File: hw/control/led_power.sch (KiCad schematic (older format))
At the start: 0 parts

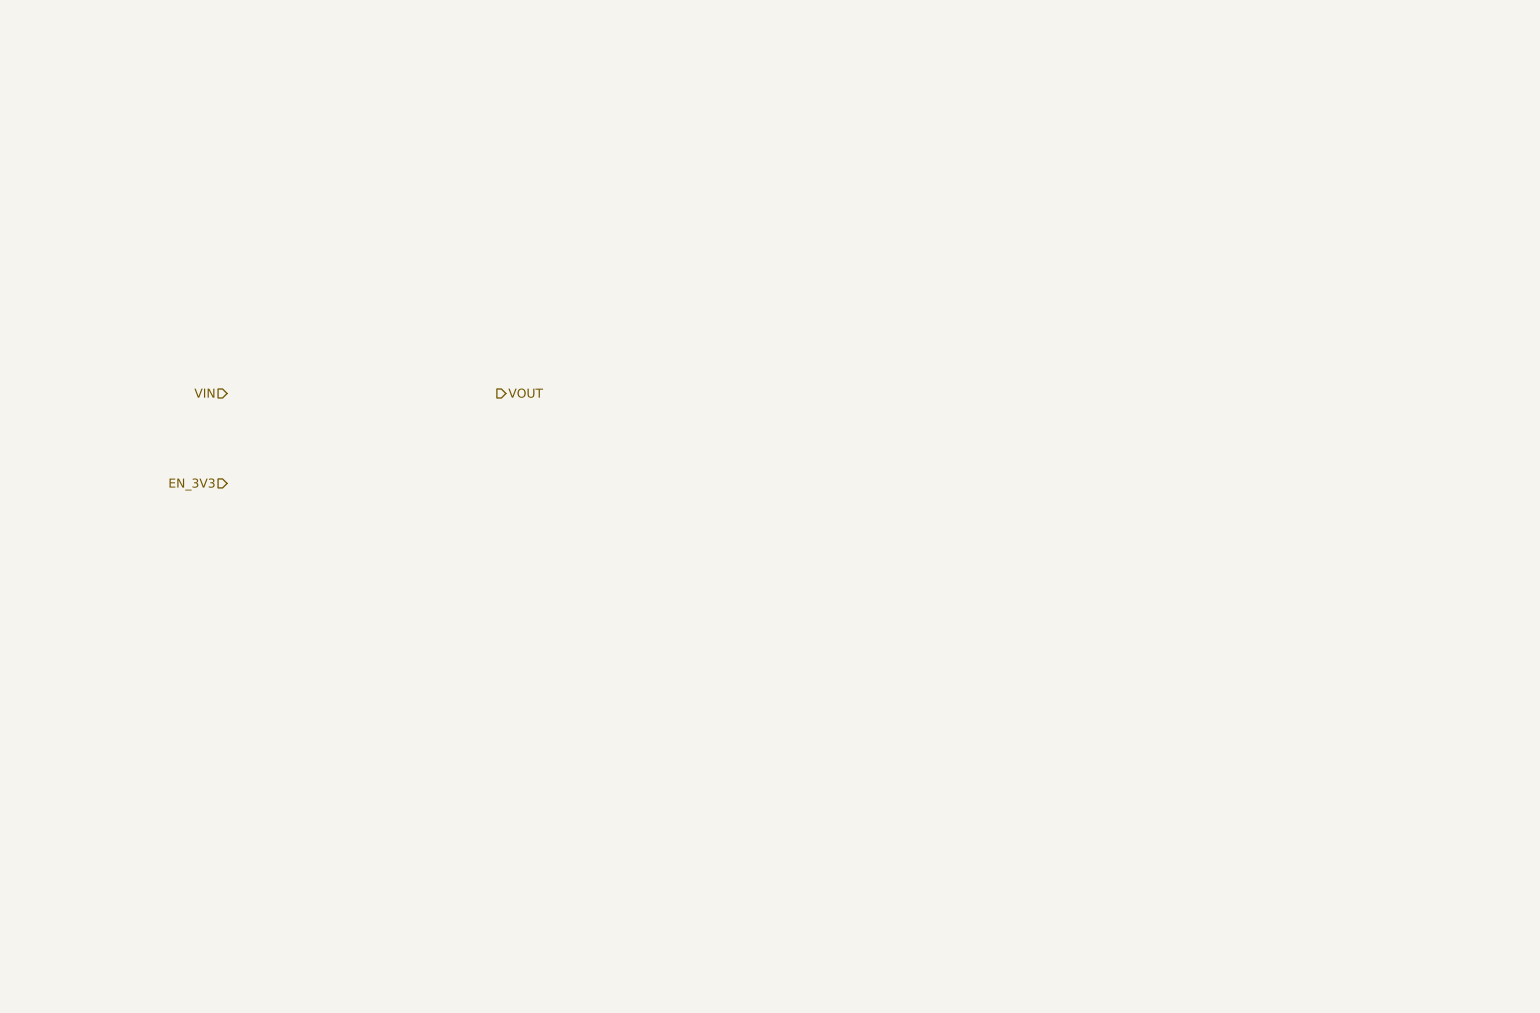
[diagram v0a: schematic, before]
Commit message: [hw] Sketch the input protection
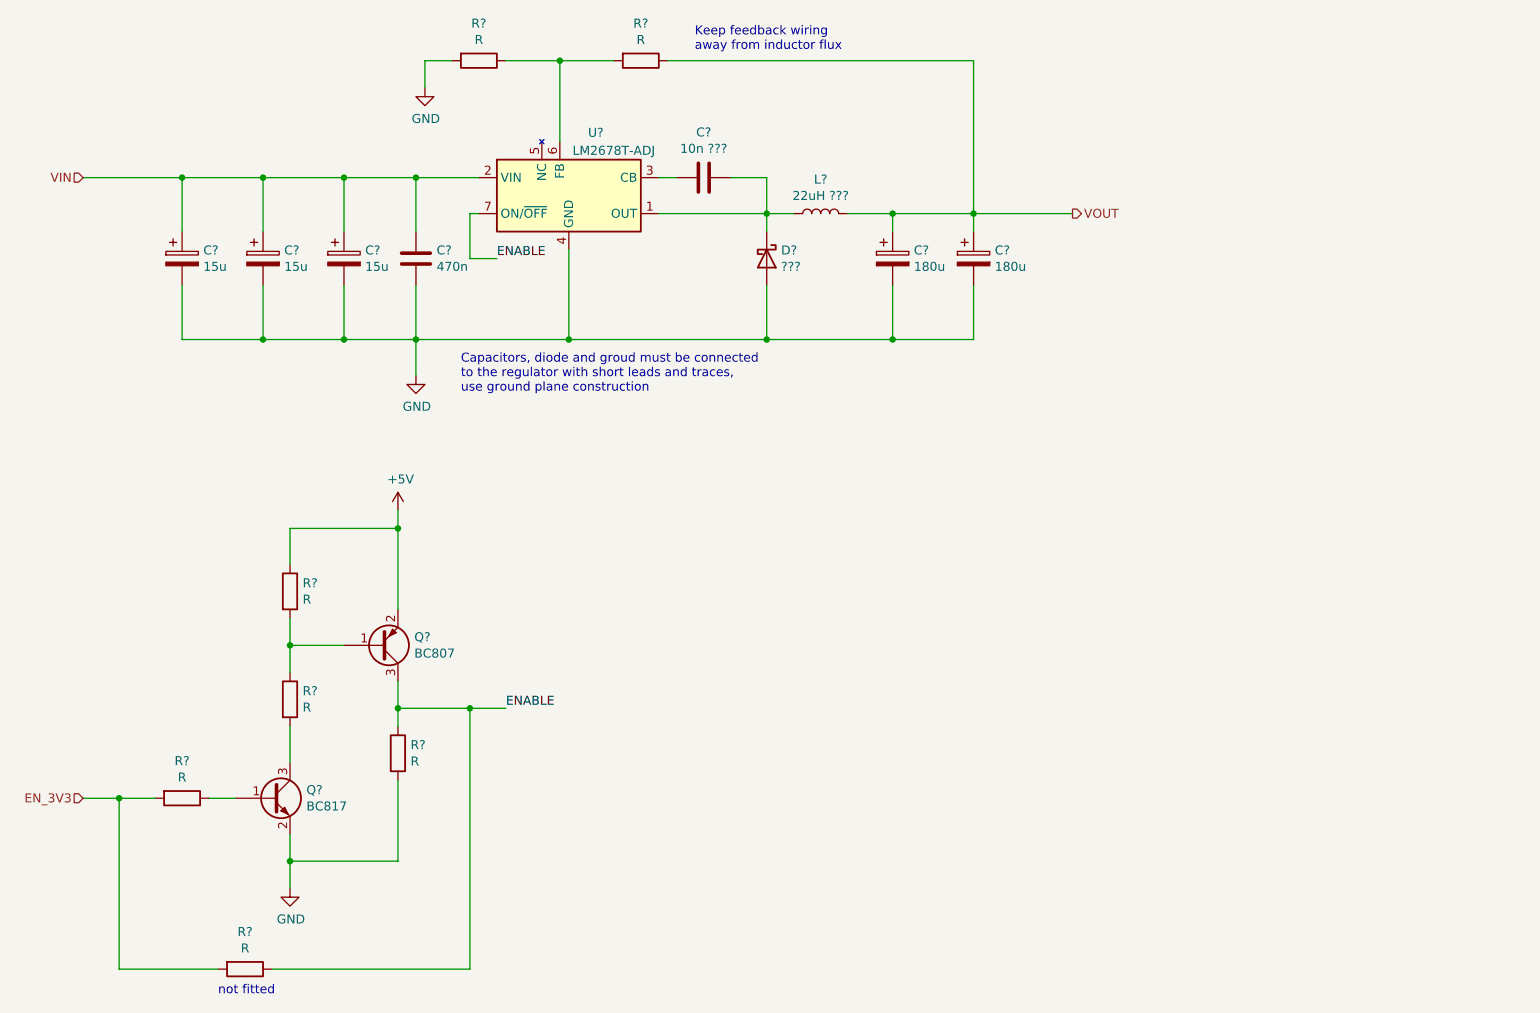
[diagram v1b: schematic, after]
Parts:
- added C?: 10n ???, symbol Device:C
- added C? (x2): 180u, symbol Device:CP
- added C? (x3): 15u, symbol Device:CP
- added C?: 470n, symbol Device:C
- added D?: ???, symbol Device:D_Schottky
- added L?: 22uH ???, symbol Device:L
- added Q?: BC817, symbol Device:Q_NPN_BEC
- added Q?: BC807, symbol Device:Q_PNP_BEC
- added R? (x7): R, symbol Device:R
- added U?: LM2678T-ADJ, Package_TO_SOT_THT:TO-220-7_P2.54x3.7mm_StaggerOdd_Lead3.8mm_Vertical, symbol my:LM2678T-ADJ
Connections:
- net EN_3V3: now also R?.2, R?.2
- net VIN: now also C?.1, C?.1, C?.1, C?.1, U?.2 (VIN)
- net VOUT: now also C?.1, C?.1, L?.2, R?.1
- new net: C?.1, D?.1 (K), L?.1, U?.1 (OUT)
- new net: C?.2, U?.3 (CB)
- new net: R?.1, R?.2, U?.6 (FB)
- new net: Q?.1 (B), R?.1
- new net: Q?.3 (C), R?.2
- new net: Q?.1 (B), R?.1, R?.2
- new net +5V: Q?.2 (E), R?.1
- new net ENABLE: Q?.3 (C), R?.1, R?.1, U?.7 (ON/~OFF~)
- new net GND: C?.2, C?.2, C?.2, C?.2, C?.2, C?.2, D?.2 (A), Q?.2 (E), R?.2, R?.2, U?.4 (GND)
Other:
- note added: "Capacitors, diode and groud must be connected\nto the regulator with short leads and traces,\nuse ground plane construction"
- note added: "Keep feedback wiring\naway from inductor flux"
- note added: "not fitted"

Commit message: [hw] Add annotations, minor fixes
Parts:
- gave numbers to parts that had none: 19

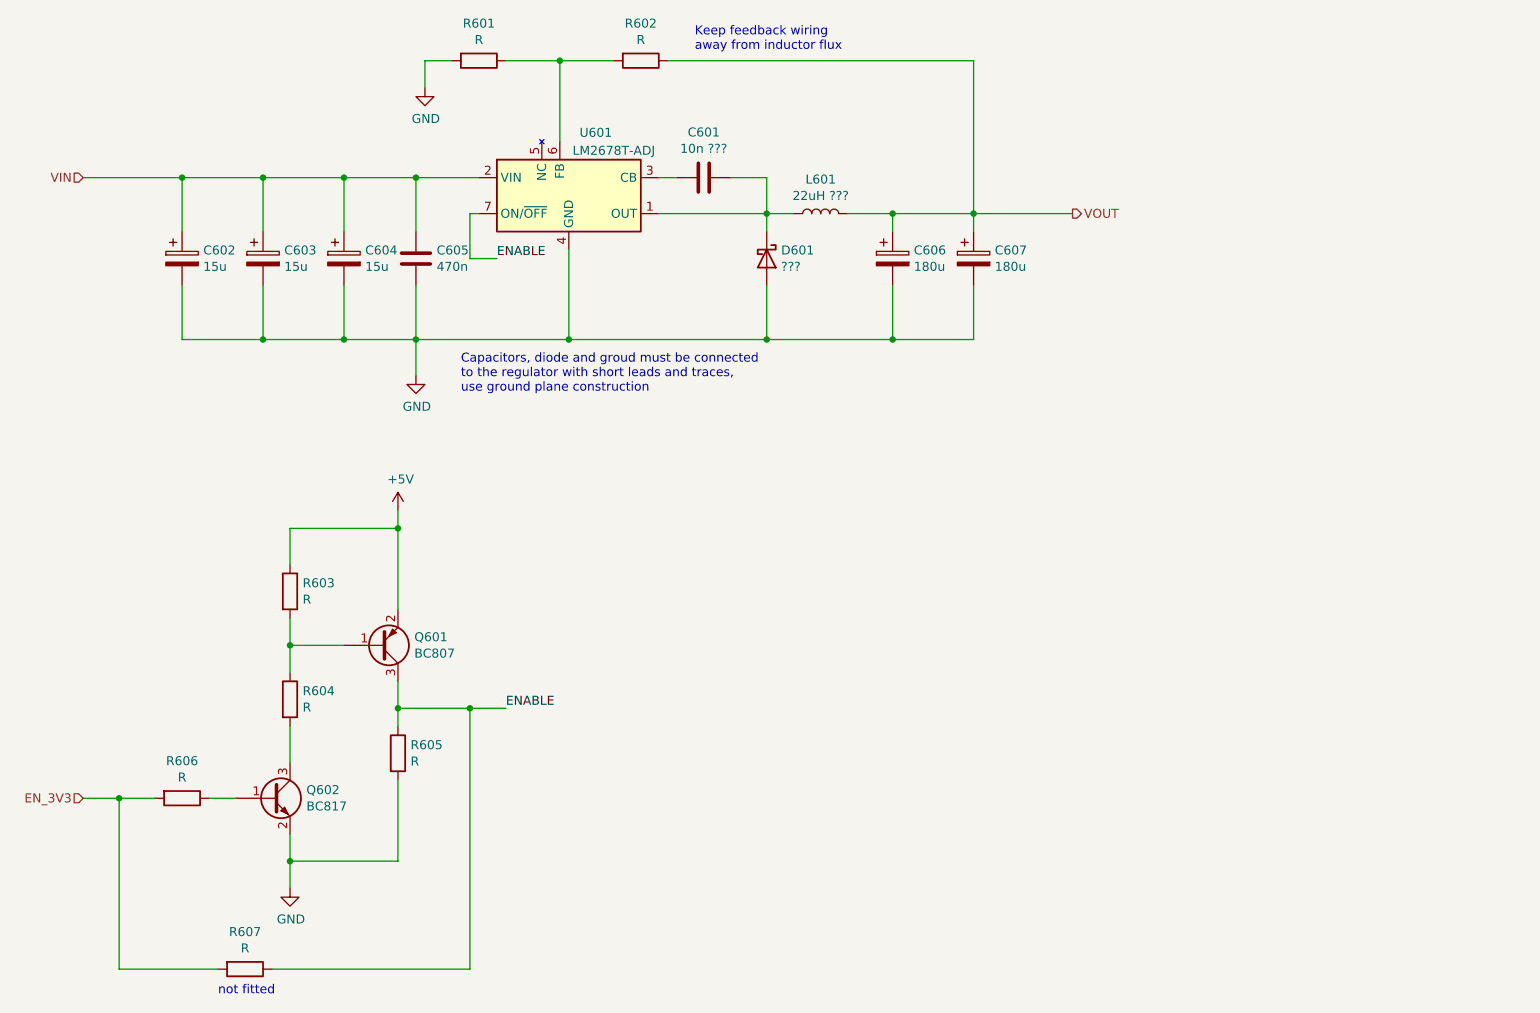
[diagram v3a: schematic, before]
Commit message: [hw] Add LED driver output sheets
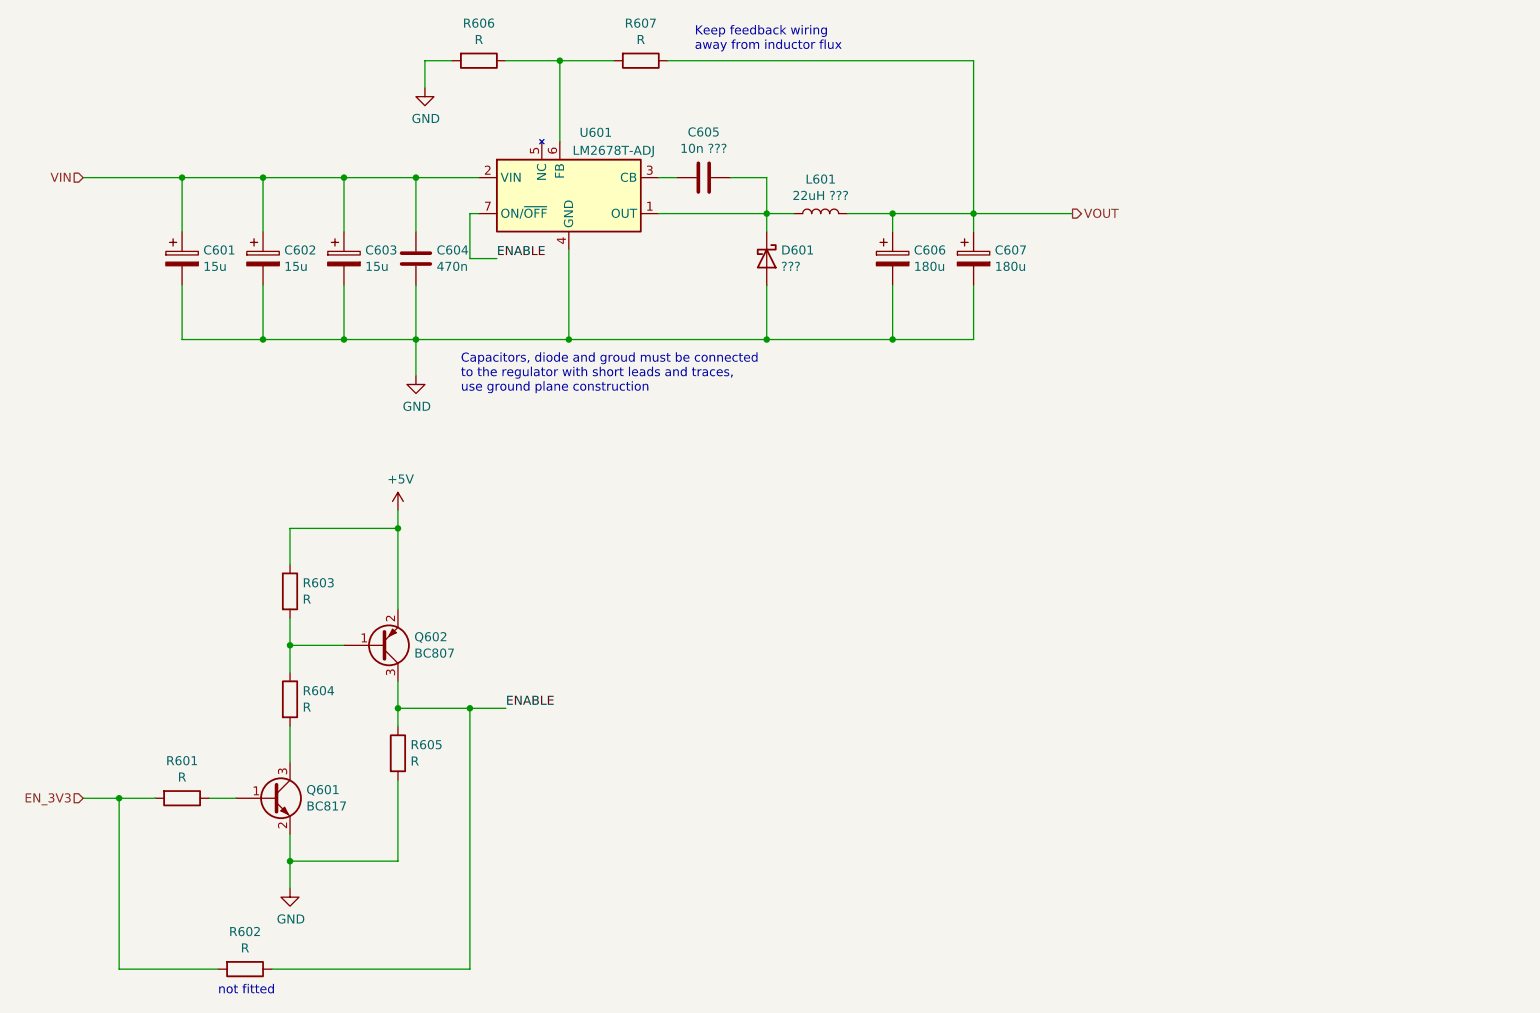
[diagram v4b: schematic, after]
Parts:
- renumbered C401 to C405, C602 to C601, C603 to C602, C604 to C603, C605 to C604, Q602 to Q601, Q601 to Q602, R606 to R601, R607 to R602, R601 to R606, R602 to R607
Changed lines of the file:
@@
 $Descr A4 11693 8268
 encoding utf-8
-Sheet 6 7
+Sheet 6 9
 Title "WS2812 Controller"
-Date "2021-09-16"
+Date "2021-09-21"
 Rev "1"
 Comp "Stefan Misik"
@@
 $EndComp
 $Comp
-L Device:C C401
+L Device:C C405
 U 1 1 6145FC0F
 P 6150 2300
-AR Path="/614AB031/6145FC0F" Ref="C401"  Part="1"
-AR Path="/614AE8DA/6145FC0F" Ref="C601"  Part="1"
-F 0 "C601" V 5898 2300 50  0000 C CNN
+AR Path="/614AB031/6145FC0F" Ref="C405"  Part="1"
+AR Path="/614AE8DA/6145FC0F" Ref="C605"  Part="1"
+F 0 "C605" V 5898 2300 50  0000 C CNN
 F 1 "10n ???" V 5989 2300 50  0000 C CNN
 F 2 "" H 6188 2150 50  0001 C CNN
@@
 	6500 2300 6300 2300
 $Comp
-L power:GND #PWR0402
+L power:GND #PWR0403
 U 1 1 61460B18
 P 4550 3400
-AR Path="/614AB031/61460B18" Ref="#PWR0402"  Part="1"
-AR Path="/614AE8DA/61460B18" Ref="#PWR0602"  Part="1"
-F 0 "#PWR0602" H 4550 3150 50  0001 C CNN
+AR Path="/614AB031/61460B18" Ref="#PWR0403"  Part="1"
+AR Path="/614AE8DA/61460B18" Ref="#PWR0603"  Part="1"
+F 0 "#PWR0603" H 4550 3150 50  0001 C CNN
 F 1 "GND" H 4555 3227 50  0000 C CNN
 F 2 "" H 4550 3400 50  0001 C CNN
@@
 $EndComp
 $Comp
-L Device:CP C604
+L Device:CP C603
 U 1 1 61465477
 P 4150 2750
-AR Path="/614AE8DA/61465477" Ref="C604"  Part="1"
-AR Path="/614AB031/61465477" Ref="C404"  Part="1"
-F 0 "C604" H 4268 2796 50  0000 L CNN
+AR Path="/614AE8DA/61465477" Ref="C603"  Part="1"
+AR Path="/614AB031/61465477" Ref="C403"  Part="1"
+F 0 "C603" H 4268 2796 50  0000 L CNN
 F 1 "15u" H 4268 2705 50  0000 L CNN
 F 2 "" H 4188 2600 50  0001 C CNN
@@
 $EndComp
 $Comp
-L Device:CP C603
+L Device:CP C602
 U 1 1 614679D1
 P 3700 2750
-AR Path="/614AE8DA/614679D1" Ref="C603"  Part="1"
-AR Path="/614AB031/614679D1" Ref="C403"  Part="1"
-F 0 "C603" H 3818 2796 50  0000 L CNN
+AR Path="/614AE8DA/614679D1" Ref="C602"  Part="1"
+AR Path="/614AB031/614679D1" Ref="C402"  Part="1"
+F 0 "C602" H 3818 2796 50  0000 L CNN
 F 1 "15u" H 3818 2705 50  0000 L CNN
 F 2 "" H 3738 2600 50  0001 C CNN
@@
 $EndComp
 $Comp
-L Device:CP C602
+L Device:CP C601
 U 1 1 61467CFC
 P 3250 2750
-AR Path="/614AE8DA/61467CFC" Ref="C602"  Part="1"
-AR Path="/614AB031/61467CFC" Ref="C402"  Part="1"
-F 0 "C602" H 3368 2796 50  0000 L CNN
+AR Path="/614AE8DA/61467CFC" Ref="C601"  Part="1"
+AR Path="/614AB031/61467CFC" Ref="C401"  Part="1"
+F 0 "C601" H 3368 2796 50  0000 L CNN
 F 1 "15u" H 3368 2705 50  0000 L CNN
 F 2 "" H 3288 2600 50  0001 C CNN
@@
 $EndComp
 $Comp
-L Device:C C605
+L Device:C C604
 U 1 1 614681BF
 P 4550 2750
-AR Path="/614AE8DA/614681BF" Ref="C605"  Part="1"
-AR Path="/614AB031/614681BF" Ref="C405"  Part="1"
-F 0 "C605" H 4665 2796 50  0000 L CNN
+AR Path="/614AE8DA/614681BF" Ref="C604"  Part="1"
+AR Path="/614AB031/614681BF" Ref="C404"  Part="1"
+F 0 "C604" H 4665 2796 50  0000 L CNN
 F 1 "470n" H 4665 2705 50  0000 L CNN
 F 2 "" H 4588 2600 50  0001 C CNN
@@
 Connection ~ 7650 2500
 $Comp
-L Device:R R602
+L Device:R R607
 U 1 1 6147393D
 P 5800 1650
-AR Path="/614AE8DA/6147393D" Ref="R602"  Part="1"
-AR Path="/614AB031/6147393D" Ref="R402"  Part="1"
-F 0 "R602" V 5593 1650 50  0000 C CNN
+AR Path="/614AE8DA/6147393D" Ref="R607"  Part="1"
+AR Path="/614AB031/6147393D" Ref="R407"  Part="1"
+F 0 "R607" V 5593 1650 50  0000 C CNN
 F 1 "R" V 5684 1650 50  0000 C CNN
 F 2 "" V 5730 1650 50  0001 C CNN
@@
 	7650 1650 7650 2500
 $Comp
-L Device:R R601
+L Device:R R606
 U 1 1 61475A47
 P 4900 1650
-AR Path="/614AE8DA/61475A47" Ref="R601"  Part="1"
-AR Path="/614AB031/61475A47" Ref="R401"  Part="1"
-F 0 "R601" V 4693 1650 50  0000 C CNN
+AR Path="/614AE8DA/61475A47" Ref="R606"  Part="1"
+AR Path="/614AB031/61475A47" Ref="R406"  Part="1"
+F 0 "R606" V 4693 1650 50  0000 C CNN
 F 1 "R" V 4784 1650 50  0000 C CNN
 F 2 "" V 4830 1650 50  0001 C CNN
@@
 	5050 1650 5350 1650
 $Comp
-L power:GND #PWR0601
+L power:GND #PWR0604
 U 1 1 61477A40
 P 4600 1800
-AR Path="/614AE8DA/61477A40" Ref="#PWR0601"  Part="1"
-AR Path="/614AB031/61477A40" Ref="#PWR0401"  Part="1"
-F 0 "#PWR0601" H 4600 1550 50  0001 C CNN
+AR Path="/614AE8DA/61477A40" Ref="#PWR0604"  Part="1"
+AR Path="/614AB031/61477A40" Ref="#PWR0404"  Part="1"
+F 0 "#PWR0604" H 4600 1550 50  0001 C CNN
 F 1 "GND" H 4605 1627 50  0000 C CNN
 F 2 "" H 4600 1800 50  0001 C CNN
@@
 Capacitors, diode and groud must be connected\nto the regulator with short leads and traces,\nuse ground plane construction
 $Comp
-L Device:R R606
+L Device:R R601
 U 1 1 6147DB7E
 P 3250 5750
-AR Path="/614AE8DA/6147DB7E" Ref="R606"  Part="1"
-AR Path="/614AB031/6147DB7E" Ref="R406"  Part="1"
-F 0 "R606" V 3043 5750 50  0000 C CNN
+AR Path="/614AE8DA/6147DB7E" Ref="R601"  Part="1"
+AR Path="/614AB031/6147DB7E" Ref="R401"  Part="1"
+F 0 "R601" V 3043 5750 50  0000 C CNN
 F 1 "R" V 3134 5750 50  0000 C CNN
 F 2 "" V 3180 5750 50  0001 C CNN
@@
 $EndComp
 $Comp
-L Device:Q_NPN_BEC Q602
+L Device:Q_NPN_BEC Q601
 U 1 1 6147EFCD
 P 3750 5750
-AR Path="/614AE8DA/6147EFCD" Ref="Q602"  Part="1"
-AR Path="/614AB031/6147EFCD" Ref="Q402"  Part="1"
-F 0 "Q602" H 3941 5796 50  0000 L CNN
+AR Path="/614AE8DA/6147EFCD" Ref="Q601"  Part="1"
+AR Path="/614AB031/6147EFCD" Ref="Q401"  Part="1"
+F 0 "Q601" H 3941 5796 50  0000 L CNN
 F 1 "BC817" H 3941 5705 50  0000 L CNN
 F 2 "" H 3950 5850 50  0001 C CNN
@@
 	3400 5750 3550 5750
 $Comp
-L Device:Q_PNP_BEC Q601
+L Device:Q_PNP_BEC Q602
 U 1 1 61480A0D
 P 4350 4900
-AR Path="/614AE8DA/61480A0D" Ref="Q601"  Part="1"
-AR Path="/614AB031/61480A0D" Ref="Q401"  Part="1"
-F 0 "Q601" H 4541 4854 50  0000 L CNN
+AR Path="/614AE8DA/61480A0D" Ref="Q602"  Part="1"
+AR Path="/614AB031/61480A0D" Ref="Q402"  Part="1"
+F 0 "Q602" H 4541 4854 50  0000 L CNN
 F 1 "BC807" H 4541 4945 50  0000 L CNN
 F 2 "" H 4550 5000 50  0001 C CNN
@@
 $EndComp
 $Comp
-L power:GND #PWR0604
+L power:GND #PWR0601
 U 1 1 61483286
 P 3850 6250
-AR Path="/614AE8DA/61483286" Ref="#PWR0604"  Part="1"
-AR Path="/614AB031/61483286" Ref="#PWR0404"  Part="1"
-F 0 "#PWR0604" H 3850 6000 50  0001 C CNN
+AR Path="/614AE8DA/61483286" Ref="#PWR0601"  Part="1"
+AR Path="/614AB031/61483286" Ref="#PWR0401"  Part="1"
+F 0 "#PWR0601" H 3850 6000 50  0001 C CNN
 F 1 "GND" H 3855 6077 50  0000 C CNN
 F 2 "" H 3850 6250 50  0001 C CNN
@@
 	3850 5050 3850 4900
 $Comp
-L power:+5V #PWR0603
+L power:+5V #PWR0602
 U 1 1 61486663
 P 4450 4150
-AR Path="/614AE8DA/61486663" Ref="#PWR0603"  Part="1"
-AR Path="/614AB031/61486663" Ref="#PWR0403"  Part="1"
-F 0 "#PWR0603" H 4450 4000 50  0001 C CNN
+AR Path="/614AE8DA/61486663" Ref="#PWR0602"  Part="1"
+AR Path="/614AB031/61486663" Ref="#PWR0402"  Part="1"
+F 0 "#PWR0602" H 4450 4000 50  0001 C CNN
 F 1 "+5V" H 4465 4323 50  0000 C CNN
 F 2 "" H 4450 4150 50  0001 C CNN
@@
 	4850 2500 4900 2500
 $Comp
-L Device:R R607
+L Device:R R602
 U 1 1 614CC1BE
 P 3600 6700
-AR Path="/614AE8DA/614CC1BE" Ref="R607"  Part="1"
-AR Path="/614AB031/614CC1BE" Ref="R407"  Part="1"
-F 0 "R607" V 3393 6700 50  0000 C CNN
+AR Path="/614AE8DA/614CC1BE" Ref="R602"  Part="1"
+AR Path="/614AB031/614CC1BE" Ref="R402"  Part="1"
+F 0 "R602" V 3393 6700 50  0000 C CNN
 F 1 "R" V 3484 6700 50  0000 C CNN
 F 2 "" V 3530 6700 50  0001 C CNN
